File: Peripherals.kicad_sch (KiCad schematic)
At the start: 43 parts, among them J5 Molex_PicoBlade_1x4_0533980471, J6 JST_SH_1x4_SM04B-SRSS-TB-LF-SN, Q3 PJE138K, Q4 PJE138K, U16 NTS0102_XSON, U17 SLB9673AU20FW2610XTMA1, U18 AP22653_DFN, U21 M24C64-F_DFN8

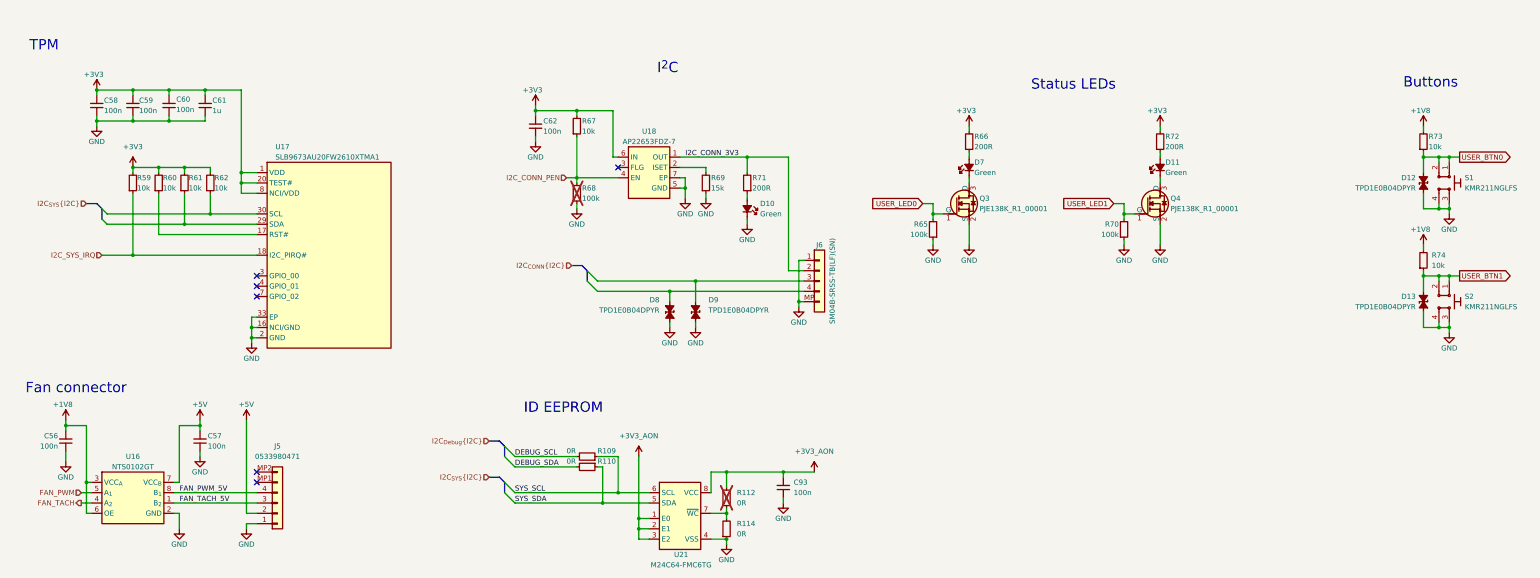
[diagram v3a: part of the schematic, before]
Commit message: [#81970] Route present on root GPIO pins on CSI and Peripherals sheets
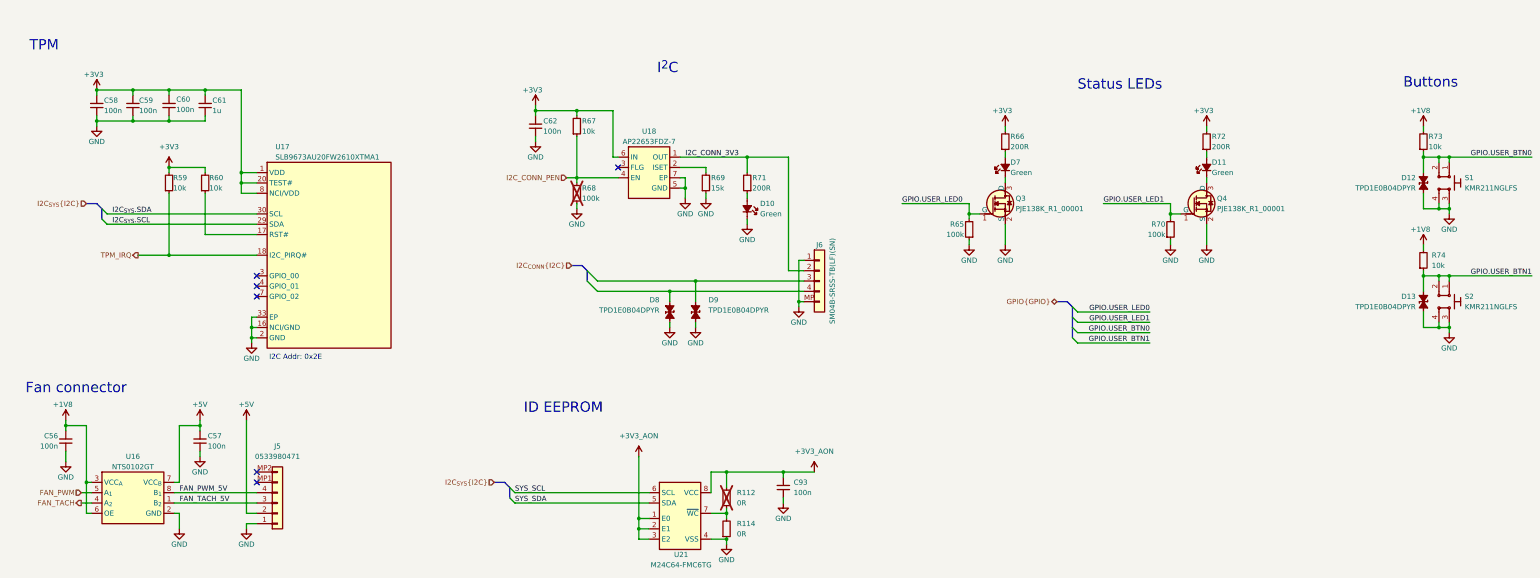
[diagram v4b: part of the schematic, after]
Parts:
- removed R109, R110: R_0R_0402, antmicro-footprints:R_0402_1005Metric, symbol antmicroResistors0402:R_0R_0402
- removed R61, R62: R_10k_0402, antmicro-footprints:R_0402_1005Metric, symbol antmicroResistors0402:R_10k_0402
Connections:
- net I2C_{SYS}.SCL: now reaches U17.29 (SDA)
- net I2C_{SYS}.SDA: now reaches U17.30 (SCL)
- net I2C_SYS_IRQ renamed TPM_IRQ
- net USER_BTN0 renamed GPIO.USER_BTN0
- net USER_BTN1 renamed GPIO.USER_BTN1
- net USER_LED0 renamed GPIO.USER_LED0
- net USER_LED1 renamed GPIO.USER_LED1
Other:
- note added: "I2C Addr: 0x2E"
- moved on the sheet: D11, D7, Q3, Q4, R59, R60, R65, R66, R70, R72

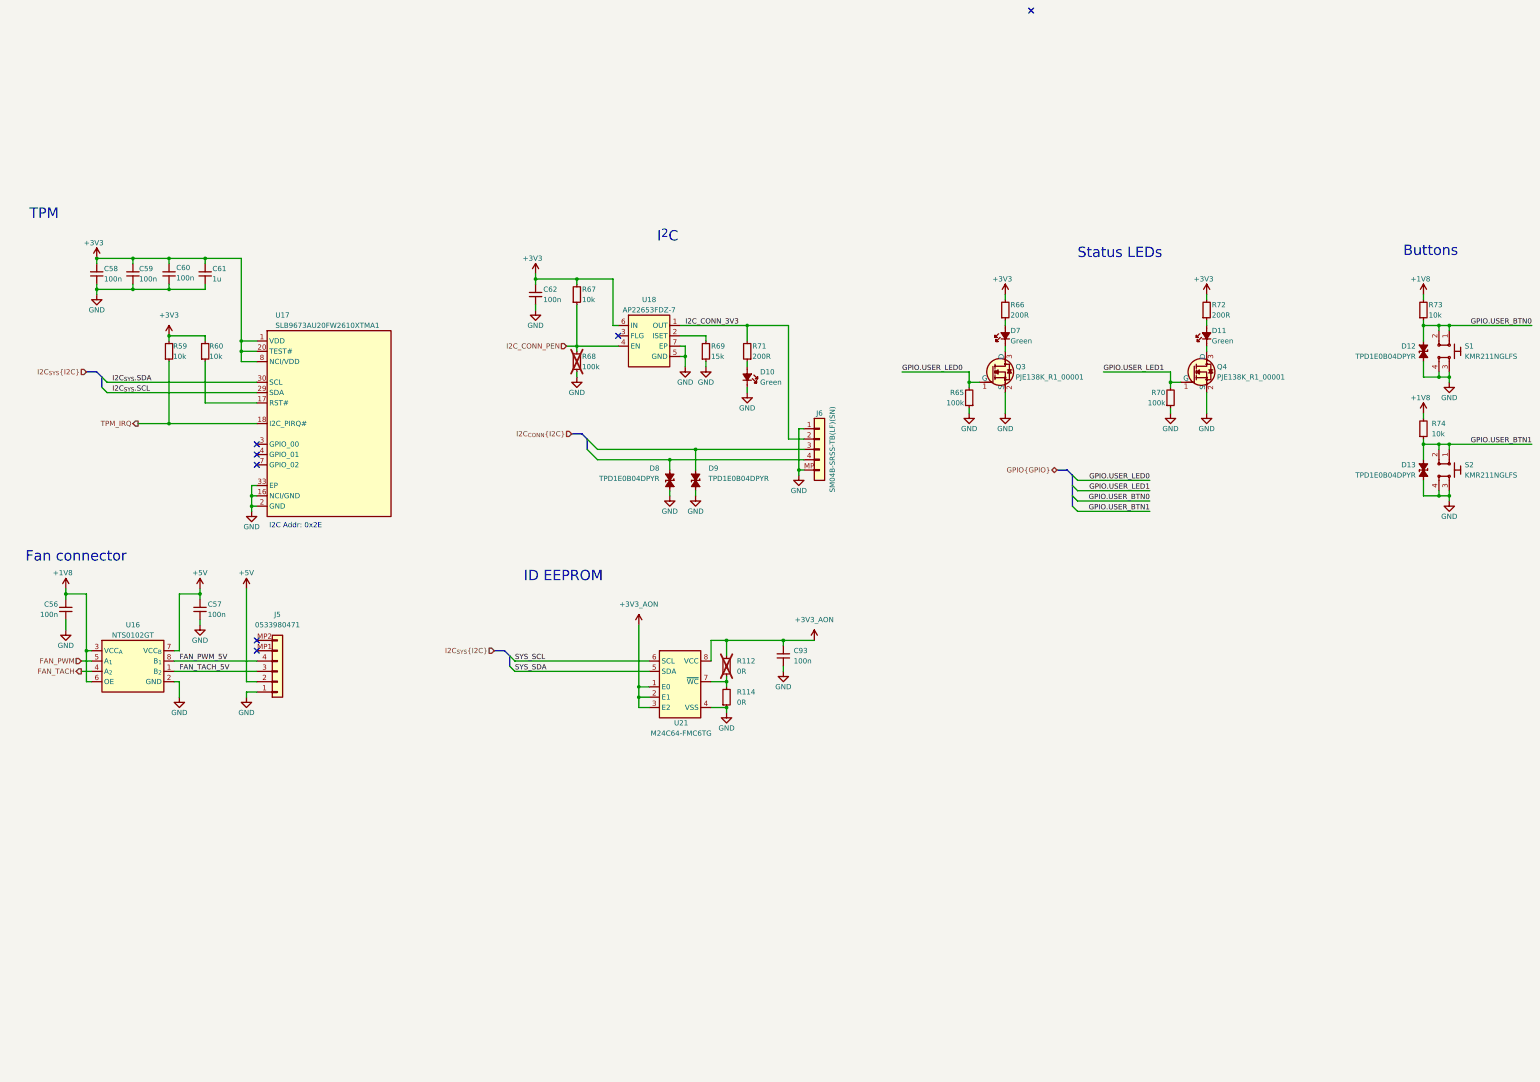
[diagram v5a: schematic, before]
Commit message: [#82057] Reorganise FMC+ pins so that they obey standard
[#82057] Add passives to expansion connector

[#82055] Clean up
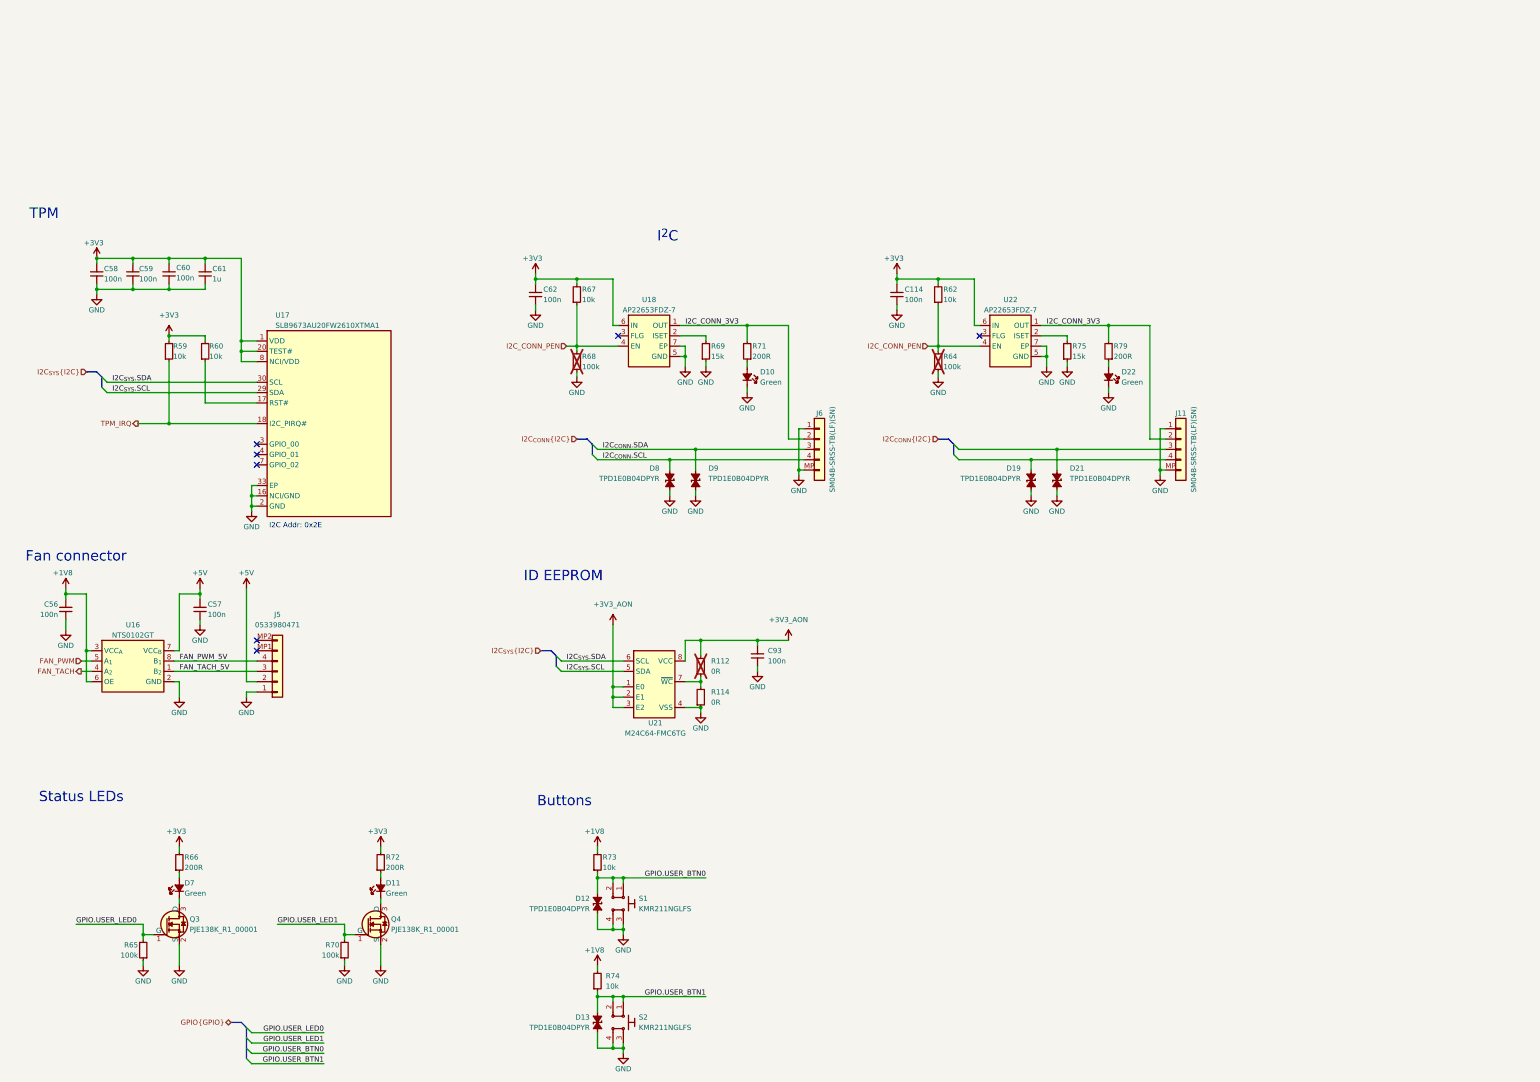
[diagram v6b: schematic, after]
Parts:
- added C114: C_100n_0402, antmicro-footprints:C_0402_1005Metric, symbol antmicroCapacitors0402:C_100n_0402
- added D19, D21: TPD1E0B04_XDFN-2, antmicro-footprints:XDFN-2_1x0.60mm, symbol antmicroTVSDiodes:TPD1E0B04_XDFN-2
- added D22: LED_G_0603_LTST-C190GKT, antmicro-footprints:LED_0603_1608Metric_G, symbol antmicroLEDIndicationDiscrete:LED_G_0603_LTST-C190GKT
- added J11: JST_SH_1x4_SM04B-SRSS-TB-LF-SN, antmicro-footprints:Conn_JST_SH_1x4_SM04B-SRSS-TB-LF-SN, symbol antmicroWire2BoardConnectors:JST_SH_1x4_SM04B-SRSS-TB-LF-SN
- added R62: R_10k_0402, antmicro-footprints:R_0402_1005Metric, symbol antmicroResistors0402:R_10k_0402
- added R64: R_100k_0402, antmicro-footprints:R_0402_1005Metric, symbol antmicroResistors0402:R_100k_0402
- added R75: R_15k_0402, antmicro-footprints:R_0402_1005Metric, symbol antmicroResistors0402:R_15k_0402
- added R79: R_200R_0402, antmicro-footprints:R_0402_1005Metric, symbol antmicroResistors0402:R_200R_0402
- added U22: AP22653_DFN, antmicro-footprints:DFN-6-1EP_2x2mm_P0.65mm_EP1x1.6mm, symbol antmicroPMICPowerDistributionSwitchesLoadDrivers:AP22653_DFN
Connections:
- net SYS_SCL is gone; now on net I2C_{SYS}.SDA: U21.6 (SCL)
- net SYS_SDA is gone; now on net I2C_{SYS}.SCL: U21.5 (SDA)
- net +3V3: now also C114.1, R62.2, U22.6 (IN)
- net GND: now also C114.2, D19.1 (C), D21.1 (C), D22.1 (C), J11.1, J11.MP, R64.1, R75.1, U22.5 (GND), U22.7 (EP)
- net I2C_CONN_3V3: now also J11.2, R79.2, U22.1 (OUT)
- net I2C_CONN_PEN: now also R62.1, R64.2, U22.4 (EN)
- net I2C_{CONN}.SCL: now reaches D8.2 (A), J6.4
- net I2C_{CONN}.SDA: now reaches D9.2 (A), J6.3
- new net: R75.2, U22.2 (ISET)
- new net: D21.2 (A), J11.3
- new net: D19.2 (A), J11.4
- new net: D22.2 (A), R79.1
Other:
- moved on the sheet: C93, D11, D12, D13, D7, Q3, Q4, R112, R114, R65, R66, R70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

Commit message: [#82757] Rename project to jetson-agx-thor-baseboard
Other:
- title: Jetson Orin AGX Baseboard -> Jetson AGX Thor Baseboard
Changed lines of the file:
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@@
 	(paper "A3")
 	(title_block
-		(title "Jetson Orin AGX Baseboard")
+		(title "Jetson AGX Thor Baseboard")
 		(date "2025-08-11")
 		(rev "1.0.0")

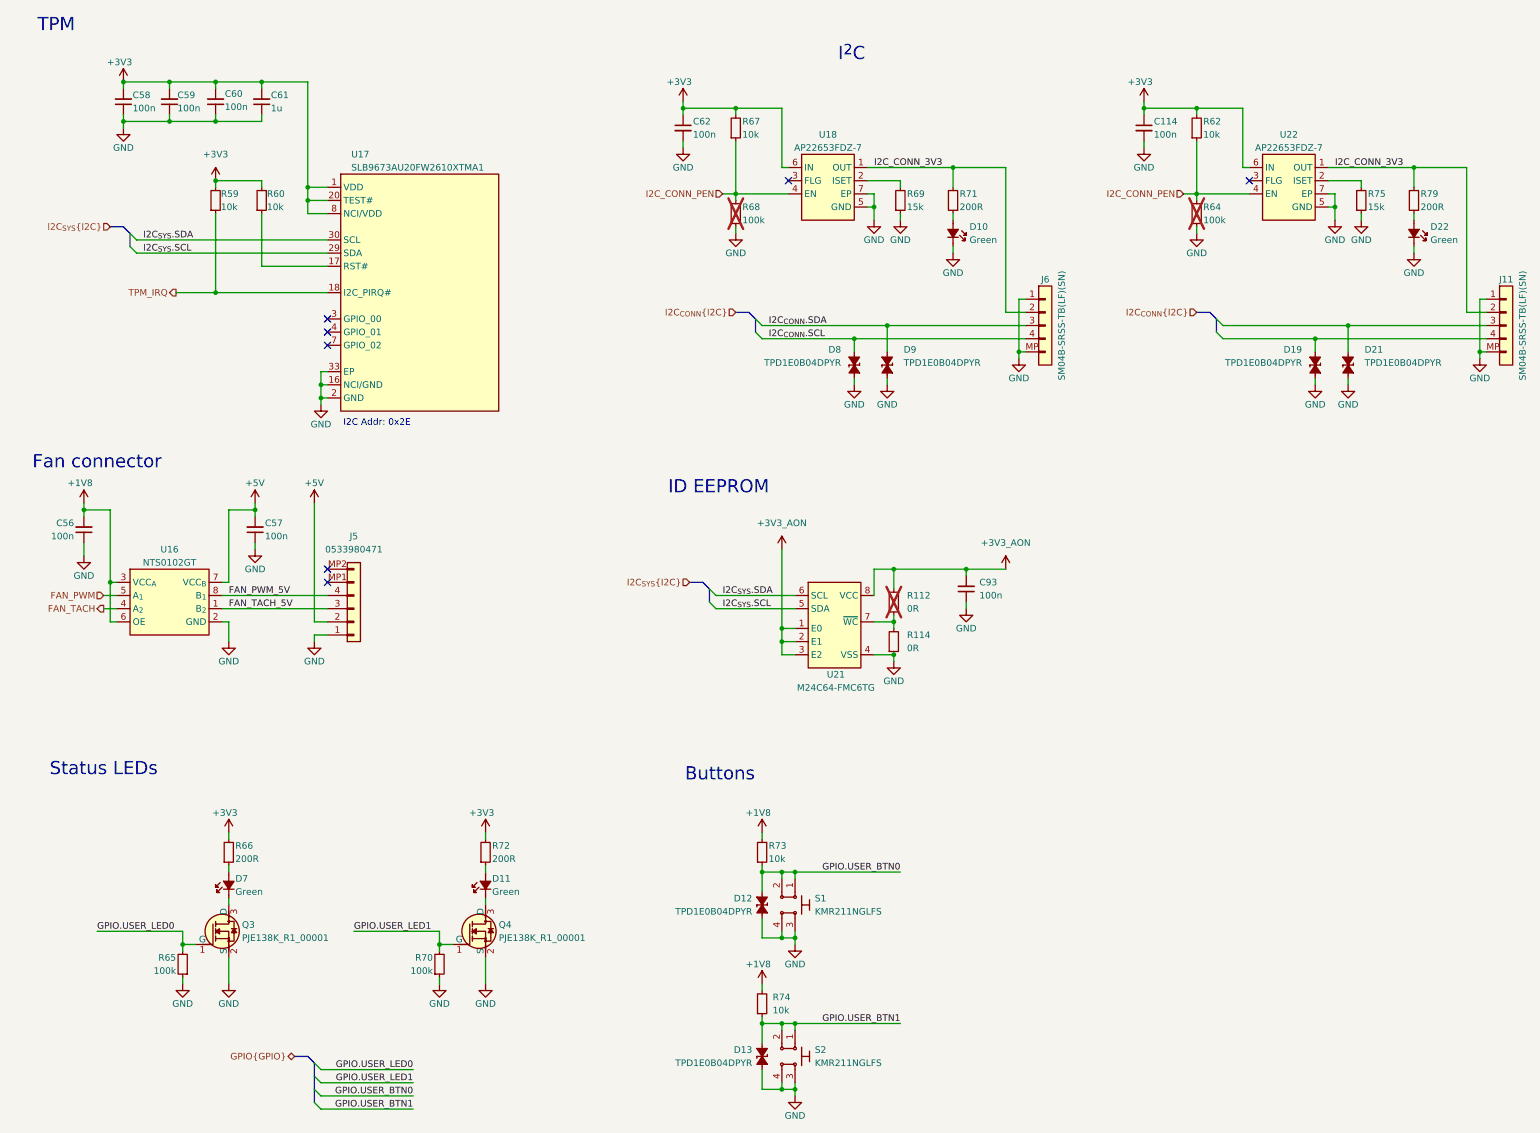
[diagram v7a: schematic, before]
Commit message: [#82757] Cleanup: reorganise page numbers and fix annotations
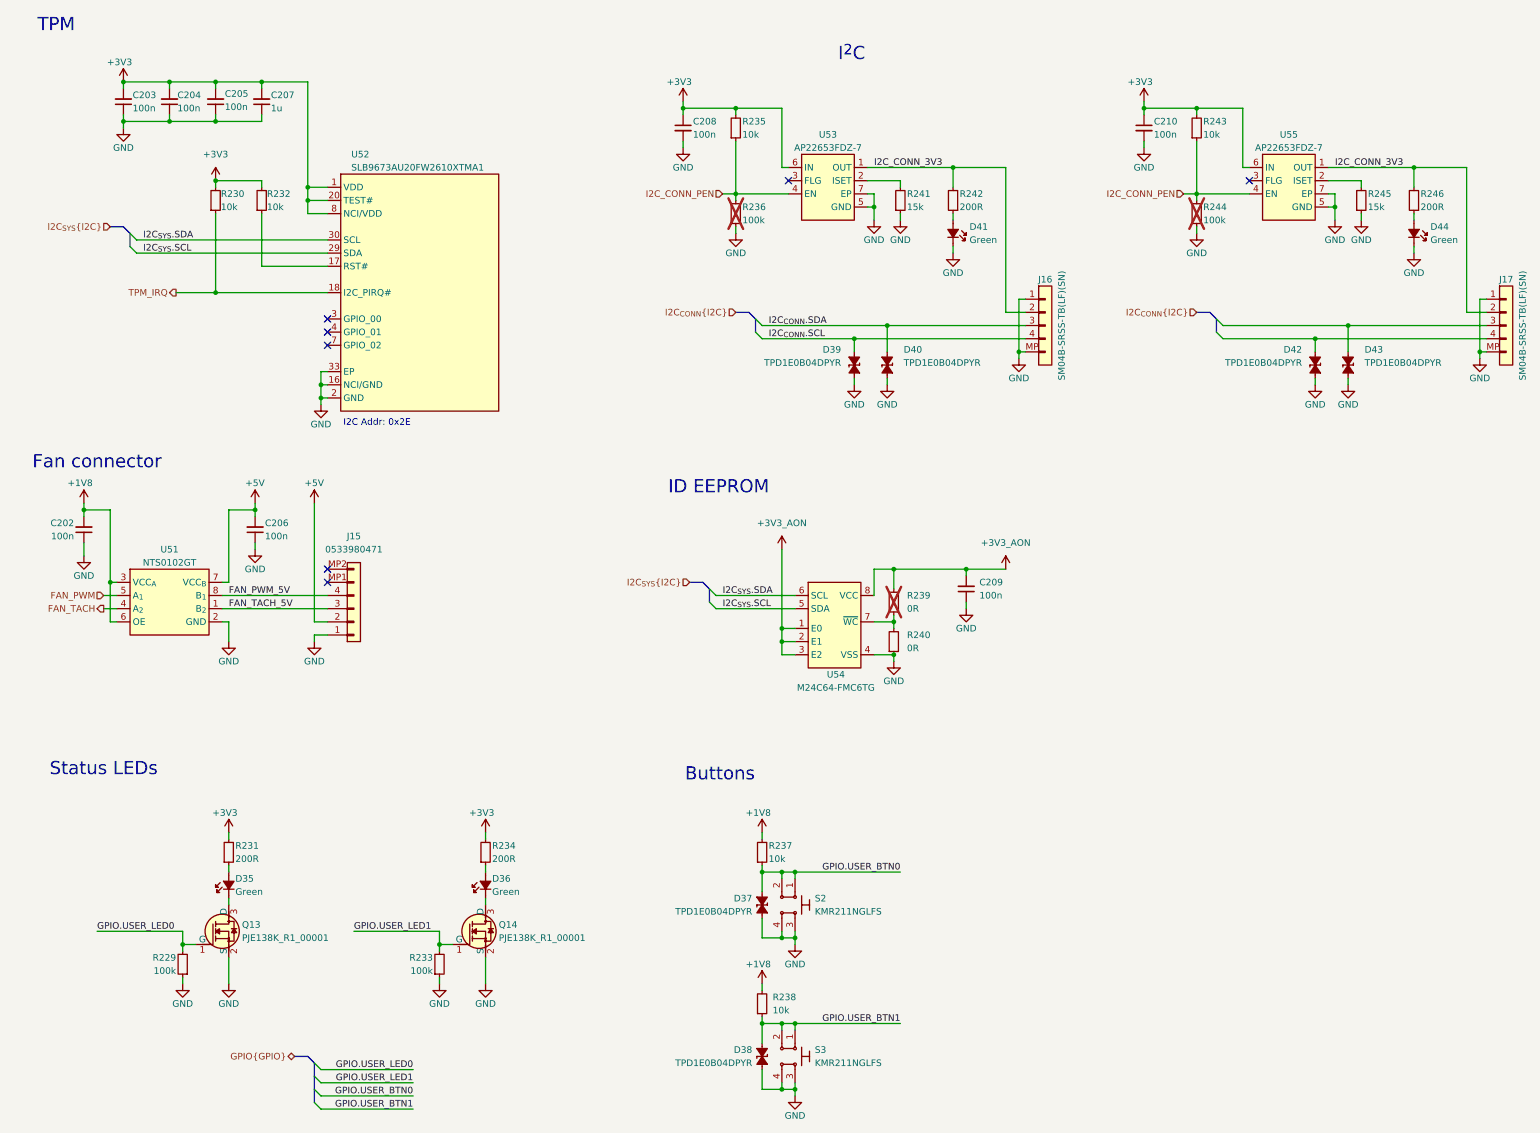
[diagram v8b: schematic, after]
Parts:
- renumbered C56 to C202, C58 to C203, C59 to C204, C60 to C205, C57 to C206, C61 to C207, C62 to C208, C93 to C209, C114 to C210, D7 to D35, D11 to D36, D12 to D37, D13 to D38, D8 to D39, D9 to D40, D10 to D41, D19 to D42, D21 to D43, D22 to D44, J5 to J15, J6 to J16, J11 to J17, Q3 to Q13, Q4 to Q14, R65 to R229, R59 to R230, R66 to R231, R60 to R232, R70 to R233, R72 to R234, R67 to R235, R68 to R236, R73 to R237, R74 to R238, R112 to R239, R114 to R240, R69 to R241, R71 to R242, R62 to R243, R64 to R244, R75 to R245, R79 to R246, S1 to S2, S2 to S3, U16 to U51, U17 to U52, U18 to U53, U21 to U54, U22 to U55
